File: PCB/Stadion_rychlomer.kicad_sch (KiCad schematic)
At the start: 64 parts, among them J1 USB_B_Micro, J2 OLED I2C, J3 ICSP, J4 Conn_01x03_Pin, J5 SPÍD & PWR, J6 AUX DDAA, J7 ENG RPM, Q1 140817143200, Q2 PC817, U1 Mikroprofesor, U2 FT232RL, U3 LM1117MP-5.0, Y1 16MHz

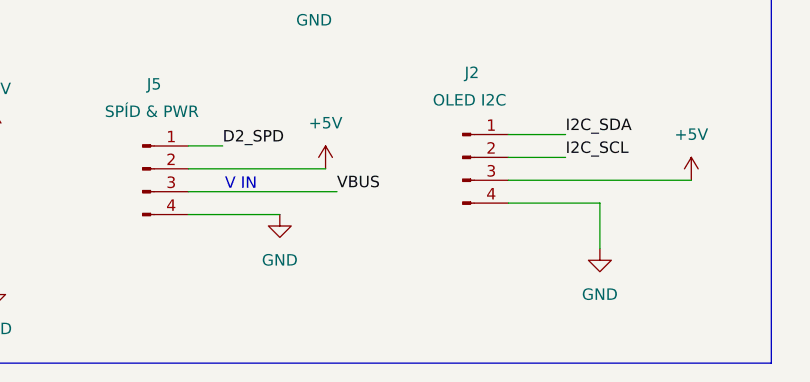
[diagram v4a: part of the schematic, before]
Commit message: Ordered in JLCPCB
Added GND Ferrite bead
Ordered in JLCPCB - stadisped.zip
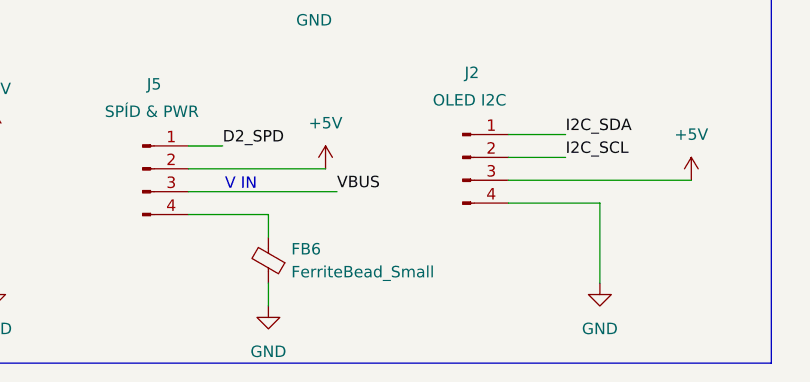
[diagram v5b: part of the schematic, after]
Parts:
- added FB6: FerriteBead_Small, Inductor_SMD:L_Panasonic_PCC-M0530M, symbol Device:FerriteBead_Small
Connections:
- net GND: now also FB6.1; no longer J5.4 (Pin_4)
- new net: FB6.2, J5.4 (Pin_4)
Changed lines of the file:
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@@
 	(wire
 		(pts
+			(xy 90.17 190.5) (xy 90.17 187.96)
+		)
+		(stroke
+			(width 0)
+			(type default)
+		)
+	)
+	(wire
+		(pts
 			(xy 116.84 90.17) (xy 121.92 90.17)
 		)
@@
 	(wire
 		(pts
+			(xy 90.17 182.88) (xy 90.17 180.34)
+		)
+		(stroke
+			(width 0)
+			(type default)
+		)
+	)
+	(wire
+		(pts
 			(xy 100.33 87.63) (xy 66.04 87.63)
 		)
@@
 	(wire
 		(pts
+			(xy 127 179.07) (xy 127 187.96)
+		)
+		(stroke
+			(width 0)
+			(type default)
+		)
+	)
+	(wire
+		(pts
 			(xy 160.02 83.82) (xy 160.02 87.63)
 		)
@@
 	(wire
 		(pts
-			(xy 81.28 180.34) (xy 91.44 180.34)
+			(xy 190.5 26.67) (xy 190.5 27.94)
 		)
 		(stroke
@@
 	(wire
 		(pts
-			(xy 190.5 26.67) (xy 190.5 27.94)
+			(xy 176.53 92.71) (xy 176.53 95.25)
 		)
 		(stroke
@@
 	(wire
 		(pts
-			(xy 176.53 92.71) (xy 176.53 95.25)
+			(xy 110.49 116.84) (xy 114.3 116.84)
 		)
 		(stroke
@@
 	(wire
 		(pts
-			(xy 110.49 116.84) (xy 114.3 116.84)
+			(xy 90.17 180.34) (xy 81.28 180.34)
 		)
 		(stroke
@@
 	(wire
 		(pts
-			(xy 127 179.07) (xy 127 184.15)
-		)
-		(stroke
-			(width 0)
-			(type default)
-		)
-	)
-	(wire
-		(pts
 			(xy 115.57 102.87) (xy 115.57 105.41)
 		)
@@
 	(symbol
 		(lib_id "power:GND")
-		(at 127 184.15 0)
+		(at 127 187.96 0)
 		(unit 1)
 		(body_style 1)
@@
 		(fields_autoplaced yes)
 		(property "Reference" "#PWR031"
-			(at 127 190.5 0)
+			(at 127 194.31 0)
 			(hide yes)
 			(show_name no)
@@
 		)
 		(property "Value" "GND"
-			(at 127 189.23 0)
+			(at 127 193.04 0)
 			(show_name no)
 			(do_not_autoplace no)
@@
 		)
 		(property "Footprint" ""
-			(at 127 184.15 0)
+			(at 127 187.96 0)
 			(hide yes)
 			(show_name no)
@@
 		)
 		(property "Datasheet" ""
-			(at 127 184.15 0)
+			(at 127 187.96 0)
 			(hide yes)
 			(show_name no)
@@
 		)
 		(property "Description" "Power symbol creates a global label with name \"GND\" , ground"
-			(at 127 184.15 0)
+			(at 127 187.96 0)
 			(hide yes)
 			(show_name no)
@@
 	)
 	(symbol
+		(lib_id "Device:FerriteBead_Small")
+		(at 90.17 185.42 180)
+		(unit 1)
+		(body_style 1)
+		(exclude_from_sim no)
+		(in_bom yes)
+		(on_board yes)
+		(in_pos_files yes)
+		(dnp no)
+		(fields_autoplaced yes)
+		(property "Reference" "FB6"
+			(at 92.71 184.188 0)
+			(show_name no)
+			(do_not_autoplace no)
+			(effects
+				(font
+					(size 1.27 1.27)
+				)
+				(justify right)
+			)
+		)
+		(property "Value" "FerriteBead_Small"
+			(at 92.71 186.728 0)
+			(show_name no)
+			(do_not_autoplace no)
+			(effects
+				(font
+					(size 1.27 1.27)
+				)
+				(justify right)
+			)
+		)
+		(property "Footprint" "Inductor_SMD:L_Panasonic_PCC-M0530M"
+			(at 91.948 185.42 90)
+			(hide yes)
+			(show_name no)
+			(do_not_autoplace no)
+			(effects
+				(font
+					(size 1.27 1.27)
+				)
+			)
+		)
+		(property "Datasheet" ""
+			(at 90.17 185.42 0)
+			(hide yes)
+			(show_name no)
+			(do_not_autoplace no)
+			(effects
+				(font
+					(size 1.27 1.27)
+				)
+			)
+		)
+		(property "Description" "Ferrite bead, small symbol"
+			(at 90.17 185.42 0)
+			(hide yes)
+			(show_name no)
+			(do_not_autoplace no)
+			(effects
+				(font
+					(size 1.27 1.27)
+				)
+			)
+		)
+		(pin "1"
+		)
+		(pin "2"
+		)
+		(instances
+			(project "Stadion_rychlomer"
+				(path "/d59b9b58-5e27-42e2-8153-65feee1218fc"
+					(reference "FB6")
+					(unit 1)
+				)
+			)
+		)
+	)
+	(symbol
 		(lib_id "power:+5V")
 		(at 261.62 134.62 0)
@@
 	(symbol
 		(lib_id "power:GND")
-		(at 91.44 180.34 0)
+		(at 90.17 190.5 0)
 		(unit 1)
 		(body_style 1)
@@
 		(fields_autoplaced yes)
 		(property "Reference" "#PWR033"
-			(at 91.44 186.69 0)
+			(at 90.17 196.85 0)
 			(hide yes)
 			(show_name no)
@@
 		)
 		(property "Value" "GND"
-			(at 91.44 185.42 0)
+			(at 90.17 195.58 0)
 			(show_name no)
 			(do_not_autoplace no)
@@
 		)
 		(property "Footprint" ""
-			(at 91.44 180.34 0)
+			(at 90.17 190.5 0)
 			(hide yes)
 			(show_name no)
@@
 		)
 		(property "Datasheet" ""
-			(at 91.44 180.34 0)
+			(at 90.17 190.5 0)
 			(hide yes)
 			(show_name no)
@@
 		)
 		(property "Description" "Power symbol creates a global label with name \"GND\" , ground"
-			(at 91.44 180.34 0)
+			(at 90.17 190.5 0)
 			(hide yes)
 			(show_name no)

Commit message: Update Silkprint a drobná škatulata
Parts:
- R2, R3: now not fitted
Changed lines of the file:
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@@
 		(on_board no)
 		(in_pos_files yes)
-		(dnp no)
+		(dnp yes)
 		(property "Reference" "R2"
 			(at 72.136 96.774 90)
@@
 		(on_board no)
 		(in_pos_files yes)
-		(dnp no)
+		(dnp yes)
 		(property "Reference" "R3"
 			(at 71.628 90.932 90)
